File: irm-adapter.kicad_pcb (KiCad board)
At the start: 2 copper layers, 82 x 40 mm, 8 parts, among them J1 , J2 

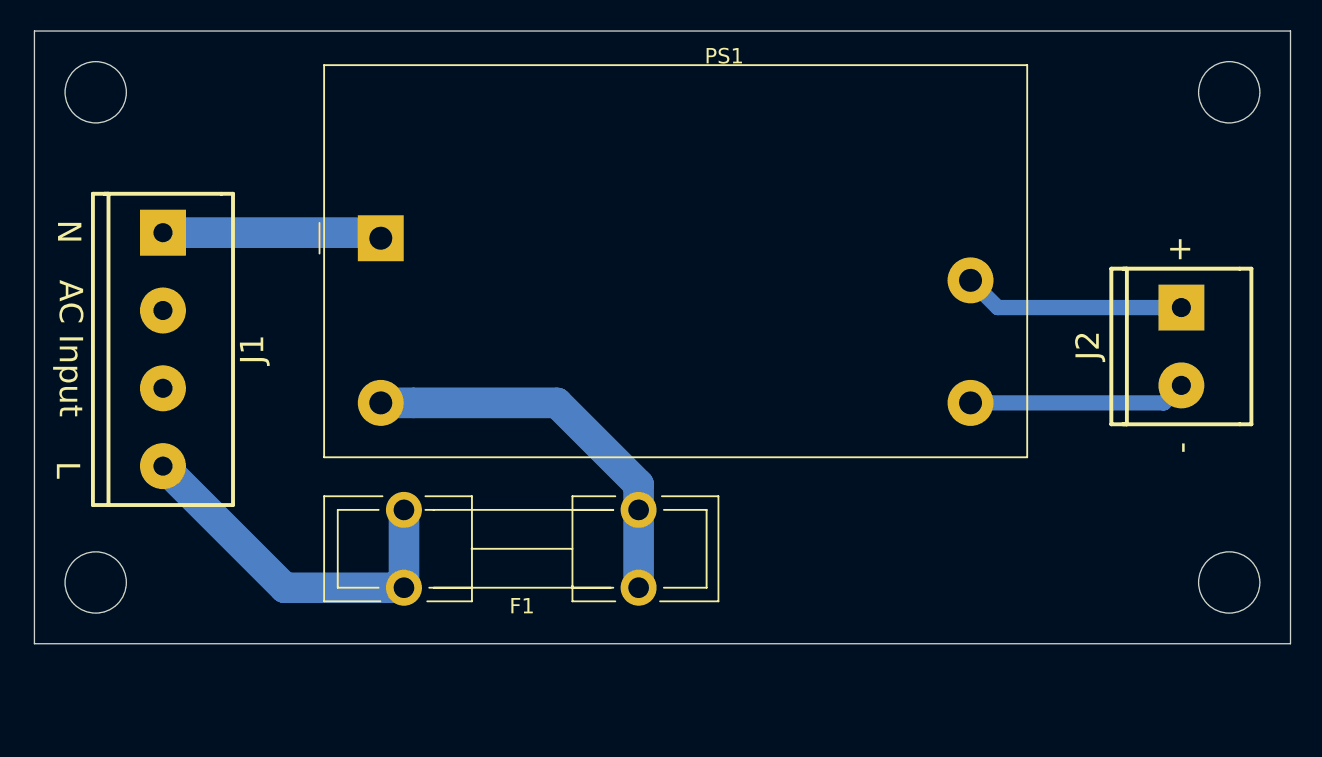
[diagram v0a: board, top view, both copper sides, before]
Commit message: added headers for Vout
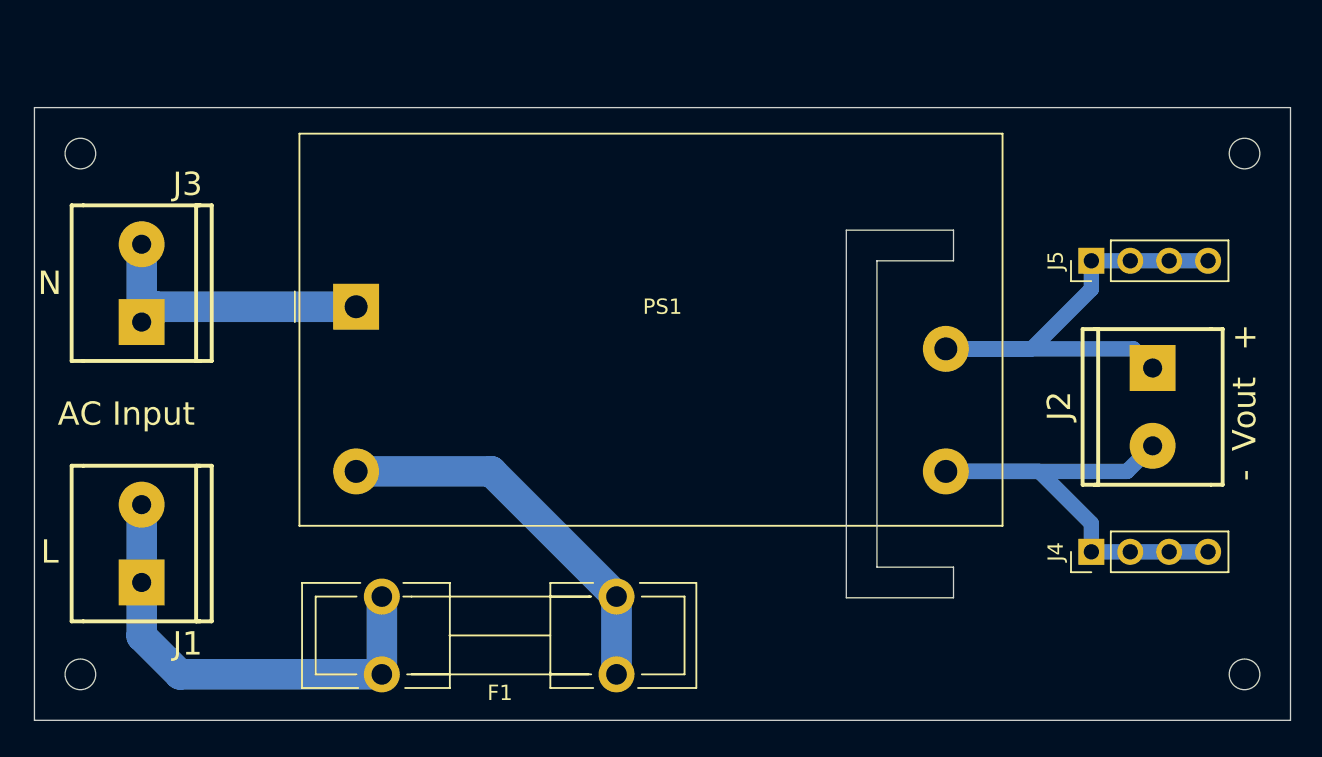
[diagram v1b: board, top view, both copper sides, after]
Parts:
- removed  : MountingHole_4mm, KiCad Footprints:MountingHole_4mm (x4)
- added ?: MountingHole_2mm, KiCad Footprints:MountingHole_2mm, F.Cu at (73.0, 77.0)
- added ?: MountingHole_2mm, KiCad Footprints:MountingHole_2mm, F.Cu at (149.0, 77.0)
- added ?: MountingHole_2mm, KiCad Footprints:MountingHole_2mm, F.Cu at (149.0, 43.0)
- added ?: MountingHole_2mm, KiCad Footprints:MountingHole_2mm, F.Cu at (73.0, 43.0)
- added J3: N, Screw Terminals:mors_2p, F.Cu at (77.0, 51.5)
- added J4: Conn_01x04_Male, Pin_Headers:Pin_Header_Straight_1x04_Pitch2.54mm, F.Cu at (139.0, 69.0)
- added J5: Conn_01x04_Male, Pin_Headers:Pin_Header_Straight_1x04_Pitch2.54mm, F.Cu at (139.0, 50.0)
- J1: value (none) -> L; footprint Screw Terminals:mors_4p -> Screw Terminals:mors_2p
- J2: value (none) -> Vout
- moved J1 12.8 mm to (77.0, 68.5), turned to 90 degrees
- moved F1 5.84 mm to (108.0, 77.0)
- moved PS1 4.75 mm to (91.0, 53.0)
- moved J2 4.37 mm to (143.0, 59.5)
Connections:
- net Net-(F1-Pad1) renamed /L_F
- net Net-(J2-Pad1) renamed /+5V
- net Net-(J2-Pad2) renamed /GND
- F1 pad 2: Net-(F1-Pad2) -> /L
- J1 pad 1: Net-(J1-Pad1) -> /L
- J1 pad 2: (no net) -> /L
- PS1 pad 1: Net-(J1-Pad1) -> /N
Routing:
- net /L: track 0.00 -> 30.4 mm
- net Net-(F1-Pad2): track 24.1 -> 0.00 mm
- net /GND: track 14.2 -> 34.6 mm
- net /+5V: track 14.5 -> 34.6 mm
- net /N: track 0.00 -> 19.5 mm
- net Net-(J1-Pad1): track 14.4 -> 0.00 mm
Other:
- outline, holes or cut-outs redrawn
- board text removed: "L"
- board text removed: "N"

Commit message: some changes
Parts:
- removed ? (x4): MountingHole_2mm, KiCad Footprints:MountingHole_2mm
- F1: footprint Fuse_Holders_and_Fuses:Fuseholder5x20_horiz_open_lateral_Type-II -> Fuse:Fuseholder_Cylinder-5x20mm_Bulgin_FX0457_Horizontal_Closed
- J1, J2, J3: footprint Screw Terminals:mors_2p -> TerminalBlock:TerminalBlock_bornier-2_P5.08mm
- J4, J5: footprint Pin_Headers:Pin_Header_Straight_1x04_Pitch2.54mm -> Connector_PinSocket_2.54mm:PinSocket_1x04_P2.54mm_Vertical
- PS1: footprint KiCad Footprints:Converter_ACDC_MeanWell_IRM-05-xx_THT -> Converter_ACDC:Converter_ACDC_MeanWell_IRM-05-xx_THT
- moved J5 27.2 mm to (145.0, 76.5), turned to 180 degrees
- moved F1 18.4 mm to (90.0, 73.0), turned to 90 degrees
- moved J4 15.0 mm to (126.0, 76.5), turned to 180 degrees
- moved J2 14.4 mm to (138.0, 73.0), turned to 180 degrees
- moved PS1 12.0 mm to (103.0, 52.0)
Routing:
- net /N: track 19.5 -> 35.5 mm
- net /L: track 30.4 -> 18.3 mm
- net /L_F: track 25.5 -> 17.2 mm
- net /GND: track 34.6 -> 29.6 mm
- net /+5V: track 34.6 -> 30.2 mm
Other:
- outline, holes or cut-outs redrawn
- board text added: "L"
- board text added: "N"

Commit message: changes
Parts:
- added J6: Conn_01x04_Female, Connector_PinSocket_2.54mm:PinSocket_1x04_P2.54mm_Vertical, F.Cu at (119.2, 76.4)
- added J7: Conn_01x04_Female, Connector_PinSocket_2.54mm:PinSocket_1x04_P2.54mm_Vertical, F.Cu at (145.5, 76.5)
- J4, J5: footprint Connector_PinSocket_2.54mm:PinSocket_1x04_P2.54mm_Vertical -> Connector_PinHeader_2.54mm:PinHeader_1x04_P2.54mm_Vertical
- moved J5 4.00 mm to (141.0, 76.5)
- moved J2 3.17 mm to (134.8, 73.0)
- moved J4 2.25 mm to (123.8, 76.5)
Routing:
- net /+5V: track 30.2 -> 60.5 mm
- net /GND: track 29.6 -> 59.5 mm
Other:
- board size 82 x 40 mm -> 80 x 40 mm
- board text added: "+ + + +"
- board text added: "- - - -"

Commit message: changes
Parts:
- J4, J5: value Conn_01x04_Male -> 1x4
- J6, J7: value Conn_01x04_Female -> 1x4
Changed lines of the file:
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@@
-(kicad_pcb (version 20171130) (host pcbnew "(5.1.0)-1")
+(kicad_pcb (version 20171130) (host pcbnew 5.1.2)
   (general
     (thickness 1.6)
@@
     (mod_text_size 1 1)
     (mod_text_width 0.15)
-    (pad_size 1.524 1.524)
-    (pad_drill 0.762)
+    (pad_size 3 3)
+    (pad_drill 1.5)
     (pad_to_mask_clearance 0.051)
     (solder_mask_min_width 0.25)
@@
     (fp_line (start 32.9 6.42) (end 32.9 -6.42) (layer F.SilkS) (width 0.12))
     (fp_line (start 32.9 6.42) (end -2.44 6.42) (layer F.SilkS) (width 0.12))
-    (pad 2 thru_hole circle (at 10.16 0 90) (size 3 3) (drill 1.35) (layers *.Cu *.Mask)
+    (pad 2 thru_hole circle (at 10.16 0 90) (size 3 3) (drill 1.5) (layers *.Cu *.Mask)
       (net 1 /L))
-    (pad 1 thru_hole circle (at 0 0 90) (size 3 3) (drill 1.35) (layers *.Cu *.Mask)
+    (pad 1 thru_hole circle (at 0 0 90) (size 3 3) (drill 1.5) (layers *.Cu *.Mask)
       (net 5 /L_F))
     (model ${KISYS3DMOD}/Fuse.3dshapes/Fuseholder_Cylinder-5x20mm_Bulgin_FX0457_Horizontal_Closed.wrl
@@
       (effects (font (size 1 1) (thickness 0.15)))
     )
-    (fp_text value Conn_01x04_Male (at 0 9.95 180) (layer F.Fab)
+    (fp_text value 1x4 (at 0 9.95 180) (layer F.Fab)
       (effects (font (size 1 1) (thickness 0.15)))
     )
@@
       (effects (font (size 1 1) (thickness 0.15)))
     )
-    (fp_text value Conn_01x04_Male (at 0 9.95 180) (layer F.Fab)
+    (fp_text value 1x4 (at 0 9.95 180) (layer F.Fab)
       (effects (font (size 1 1) (thickness 0.15)))
     )
@@
       (effects (font (size 1 1) (thickness 0.15)))
     )
-    (fp_text value Conn_01x04_Female (at 0 10.39 180) (layer F.Fab)
+    (fp_text value 1x4 (at 0 10.39 180) (layer F.Fab)
       (effects (font (size 1 1) (thickness 0.15)))
     )
@@
       (effects (font (size 1 1) (thickness 0.15)))
     )
-    (fp_text value Conn_01x04_Female (at 0 10.39 180) (layer F.Fab)
-      (effects (font (size 1 1) (thickness 0.15)))
-    )
+    (fp_text value 1x4 (at 0 10.39 180) (layer F.Fab)
+      (effects (font (size 1 1) (thickness 0.15)))
+    )
